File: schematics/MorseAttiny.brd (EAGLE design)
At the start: 71.1 x 41.9 mm, 12 parts, among them Q1 500mA/300V

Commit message: no message
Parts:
- moved R1 38.2 mm to (20.7, 35.8), turned to 200.3 degrees
- moved J1 30.0 mm to (43.3, 10.1), turned to 159.8 degrees
- moved R2 23.3 mm to (17.3, 6.14), turned to 203.6 degrees
- moved PAD1 19.4 mm to (49.0, 23.2)
- moved PAD4 18.7 mm to (55.0, 18.8)
- moved PAD2 15.8 mm to (55.0, 23.1)
- moved C1 13.8 mm to (25.4, 20.9), turned to 89.9 degrees
- moved PAD3 12.6 mm to (49.0, 18.8)
- moved D1 8.98 mm to (14.8, 26.3), turned to 200.8 degrees
- moved Q1 6.48 mm to (63.0, 20.9), turned to 87.7 degrees
- moved D2 6.22 mm to (14.6, 15.9), turned to 338.6 degrees
- moved U$1 2.42 mm to (35.4, 21.6)
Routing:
- net VCC: track 96.8 -> 252.0 mm, vias 0 -> 3
- net N$3: track 59.4 -> 15.3 mm, vias 2 -> 0
- net N$4: track 24.4 -> 54.8 mm, vias 2 -> 0
- net RESET: track 47.5 -> 20.5 mm
- net N$1: track 66.1 -> 90.8 mm
- net SCK: track 45.8 -> 26.5 mm
- net N$2: track 7.53 -> 24.5 mm
- net MISO: track 33.5 -> 17.6 mm
- net GND: track 135.2 -> 150.2 mm, vias 0 -> 4
- net N$5: track 54.0 -> 42.8 mm
- net MOSI: track 28.9 -> 37.3 mm
- net N$7: track 20.4 -> 19.7 mm, vias 0 -> 2

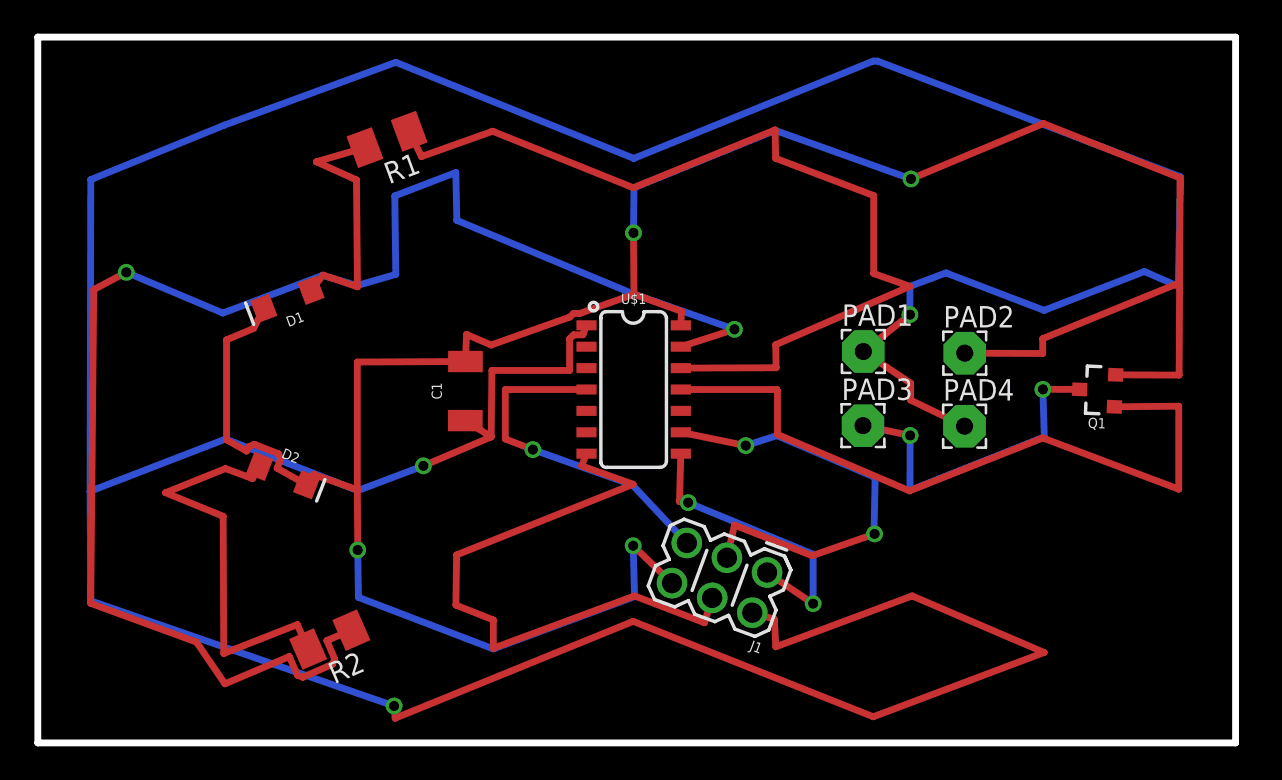
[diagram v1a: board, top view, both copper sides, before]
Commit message: Major changes in Illustrator design and first silkscreen experiments
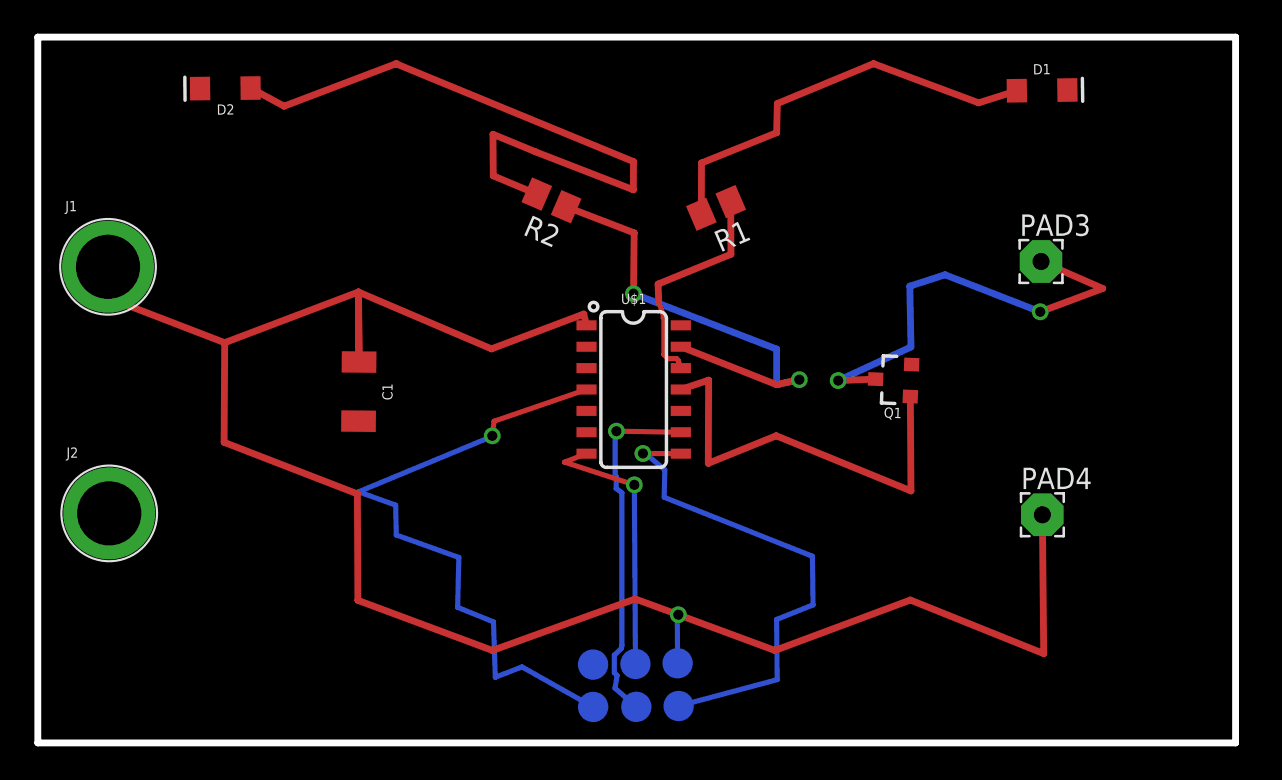
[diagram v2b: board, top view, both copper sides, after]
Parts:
- removed PAD1, PAD2: (no value), wirepad:2,54/1,0
- added J2: (no value), SparkFun-Connectors:BANANA_CONN
- added TP1, TP2, TP3, TP4, TP5, TP7: TPTP18R, testpad:TP18R
- J1: device SparkFun-Connectors:2X3_POGO -> SparkFun-Connectors:BANANA_CONN
- R1, R2: device rcl:M1206 -> rcl:M0805
- moved D1 46.5 mm to (59.6, 38.7), turned to 0.8 degrees
- moved J1 43.1 mm to (4.17, 28.3), turned to 0 degrees
- moved R2 29.2 mm to (30.5, 32.2), turned to 156.7 degrees
- moved D2 23.2 mm to (11.1, 38.9), turned to 180.6 degrees
- moved R1 20.0 mm to (40.3, 31.8), turned to 203.2 degrees
- moved PAD3 14.4 mm to (59.6, 28.6)
- moved Q1 12.1 mm to (50.8, 21.6)
- moved PAD4 7.00 mm to (59.6, 13.5)
- moved C1 6.33 mm to (19.1, 20.9), turned to 269.5 degrees
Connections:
- net GND: now also J2.P$1, TP7.TP; no longer J1.P$6, PAD2.1
- net MISO: now also TP5.TP; no longer J1.P$1
- net MOSI: now also TP1.TP; no longer J1.P$4
- net RESET: now also TP3.TP; no longer J1.P$5
- net SCK: now also TP4.TP; no longer J1.P$3
- net VCC: now also J1.P$1, TP2.TP; no longer J1.P$2, PAD1.1
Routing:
- net GND: track 150.2 -> 0.00 mm, vias 4 -> 0
- net VCC: track 252.0 -> 116.7 mm, vias 3 -> 1
- net N$1: track 90.8 -> 28.5 mm
- net N$4: track 54.8 -> 13.5 mm
- net MOSI: track 37.3 -> 16.4 mm, vias 0 -> 1
- net RESET: track 20.5 -> 38.6 mm
- net N$5: track 42.8 -> 25.3 mm
- net N$2: track 24.5 -> 40.5 mm
- net MISO: track 17.6 -> 29.9 mm, vias 2 -> 1
- net N$3: track 15.3 -> 24.8 mm
- net N$7: track 19.7 -> 26.8 mm
- net SCK: track 26.5 -> 21.5 mm, vias 2 -> 1
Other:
- board text added: "-.. .. --. .. - .- .-.."
- board text added: ".. -.. . .- - .. --- -."

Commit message: changed pads to polygon areas, added eagle up renderings, major re-design
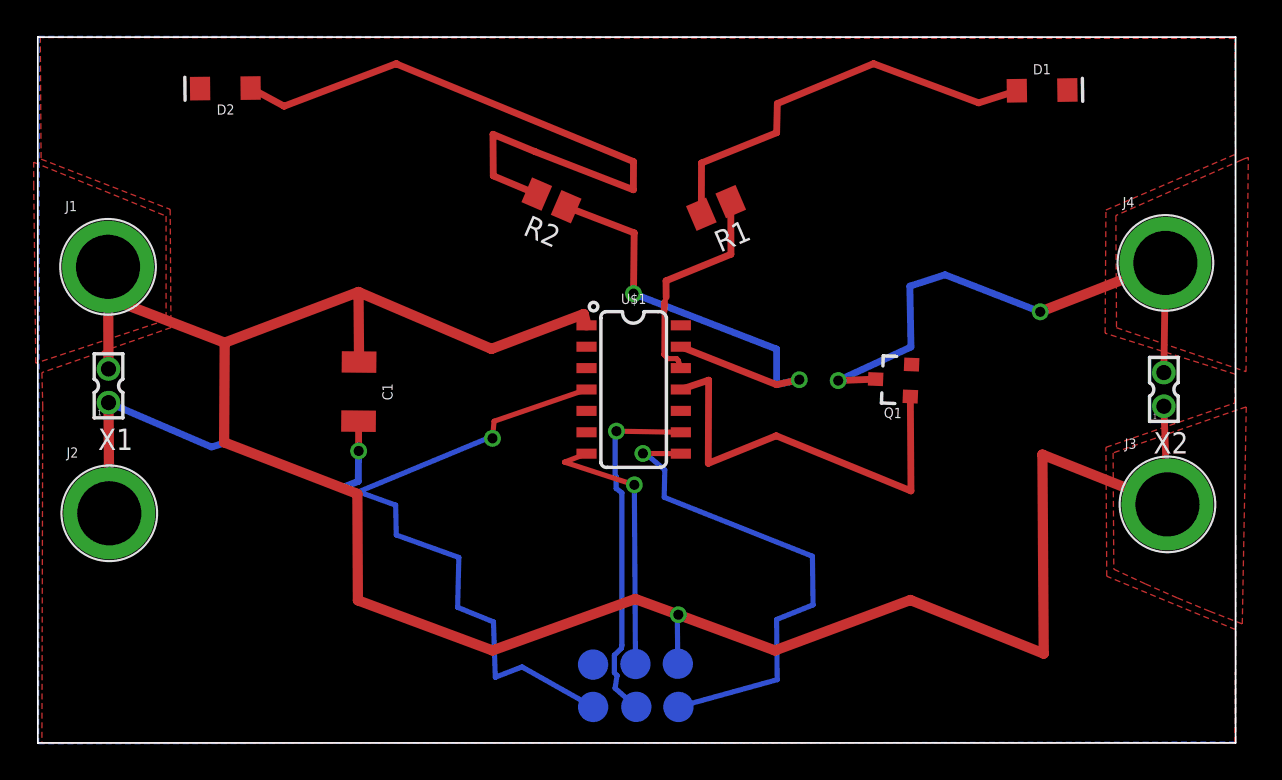
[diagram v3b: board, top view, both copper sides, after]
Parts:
- removed PAD3, PAD4: (no value), wirepad:2,54/1,0
- added J3, J4: (no value), SparkFun-Connectors:BANANA_CONN
- added X1, X2: 332-02, con-garry:332-02
- R1, R2: value (none) -> 220r
- moved TP5 0.06 mm to (38.0, 2.14)
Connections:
- removed net N$7: PAD3.1, Q1.3
- new net SPK: J4.P$1, Q1.3, X2.2
- net GND: now also X1.1
- net VCC: now also J3.P$1, X1.2, X2.1; no longer PAD4.1
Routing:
- net SPK: track 0.00 -> 33.3 mm, vias 0 -> 2
- net N$7: track 26.8 -> 0.00 mm, vias 2 -> 0
- net GND: track 0.00 -> 26.4 mm, vias 0 -> 1
- net VCC: track 116.7 -> 140.1 mm
- added copper zone on layer 1, net SPK
- added copper zone on layer 1, net VCC
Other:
- board text added: "+"
- board text added: "-"

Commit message: minor cleanups, first gerber files
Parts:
- moved Q1 0.98 mm to (51.8, 21.6), turned to 90 degrees
- moved J3 0.64 mm to (67.4, 13.6)
- moved J4 0.63 mm to (67.5, 28.2)
- moved J1 0.43 mm to (3.74, 28.3)
- moved J2 0.36 mm to (3.89, 13.6)
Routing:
- net SPK: track 33.3 -> 29.2 mm
- net N$1: track 28.5 -> 25.9 mm
- net VCC: track 140.1 -> 141.4 mm
- net N$5: track 25.3 -> 26.0 mm
